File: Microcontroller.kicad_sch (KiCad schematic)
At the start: 33 parts, among them J501 USB4105-GF-A, J502 TC2030-CTX, SW501 PTS526SK15SMTR2 LFS, U501 USBLC6-2SC6, U502 STM32G441KBT6, Y501 ATS08A-E

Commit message: feat: checked REV A
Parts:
- removed J502: TC2030-CTX, Connector:Tag-Connect_TC2030-IDC-NL_2x03_P1.27mm_Vertical, symbol Connector:Conn_ARM_SWD_TagConnect_TC2030-NL
- added F501: MF-MSMF030-2, Resistor_SMD:R_1812_4532Metric, symbol Device:Polyfuse_Small
- added J501: Conn_ST_STDC14, Connector_PinHeader_1.27mm:PinHeader_2x07_P1.27mm_Vertical_SMD, symbol Connector:Conn_ST_STDC14
- FB501: value ?UNKWN? -> MH1608-601Y; footprint (none) -> Inductor_SMD:L_0603_1608Metric; Impedance (none) -> 600R @ 100MHz; MPN (none) -> MH1608-601Y; Manufacturer (none) -> Bourns Inc.; SPN (none) -> MH1608-601YCT-ND; Supplier (none) -> DigiKey
- renumbered C506 to C504, C504 to C505, C507 to C506, C508 to C507, C505 to C508, C515 to C510, C516 to C511, C510 to C512, J501 to J502, R510 to R503, R509 to R504, R507 to R505, R508 to R506, R503 to R507, R505 to R508, R504 to R509, R506 to R510, U502 to U501, U501 to U502
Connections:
- net +3V0: now also J501.3 (VCC)
- net GND: now also J501.5 (GND), J501.7 (GND)
- net VBUS: now also F501.2; no longer J502.A4 (VBUS), J502.A9 (VBUS), J502.B4 (VBUS), J502.B9 (VBUS)
- net at R504.1: now also J501.4 (JTMS/SWDIO)
- net at R505.1: now also J501.12 (~{RST})
- net at R503.1: now also J501.6 (JCLK/SWCLK)
- net at R506.1: now also J501.8 (JTDO/SWO)
- new net VBUS_RAW: F501.1, J502.A4 (VBUS), J502.A9 (VBUS), J502.B4 (VBUS), J502.B9 (VBUS)
- no-connect marks 12 -> 17
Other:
- note removed: "Unknown if there is an available part"
- moved on the sheet: C501, C502, C503, C504, C505, C506, C507, C508, C509, C510, C511, C512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

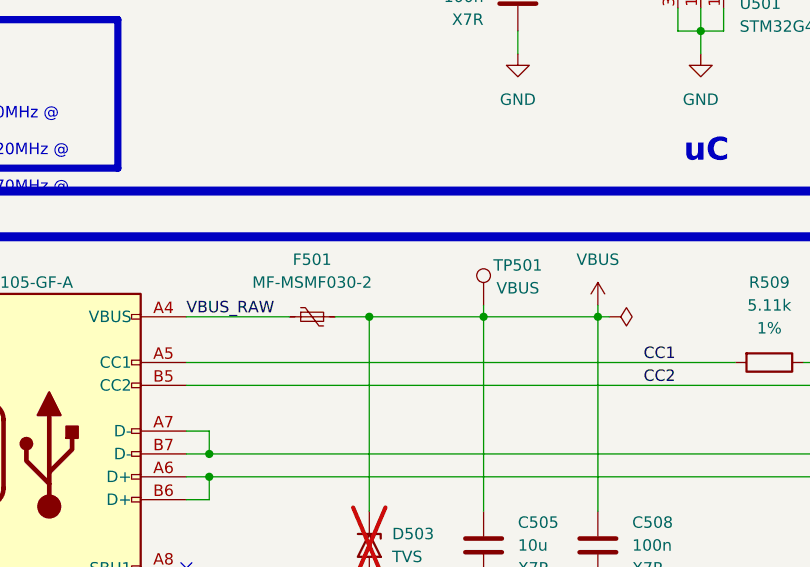
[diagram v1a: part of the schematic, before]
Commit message: fix: net naming, NC STM32 pins, silkscreen, pin 1 indicator
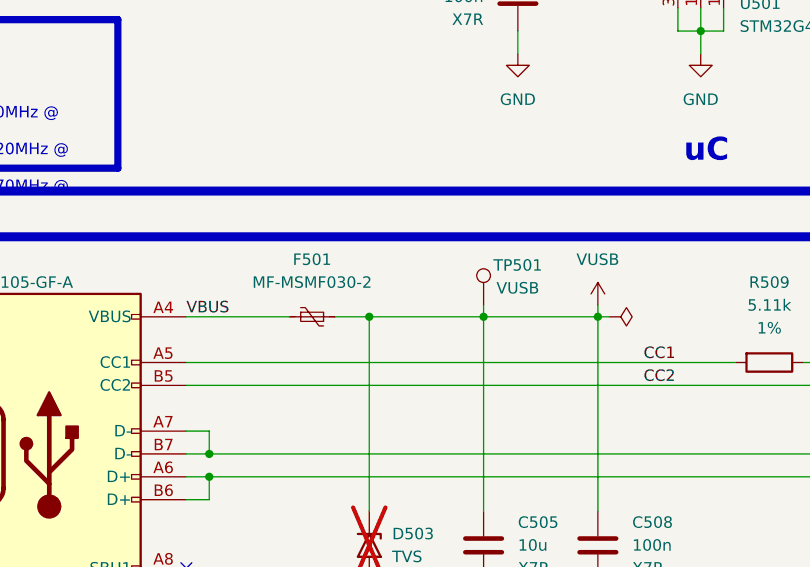
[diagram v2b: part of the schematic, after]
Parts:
- TP501: value VBUS -> VUSB
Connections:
- net VBUS_RAW is gone; now on net VBUS: F501.1, J502.A4 (VBUS), J502.A9 (VBUS), J502.B4 (VBUS), J502.B9 (VBUS)
- net VBUS: no longer C505.1, C508.1, D503.1 (A1), F501.2, TP501.1
- new net VUSB: C505.1, C508.1, D503.1 (A1), F501.2, TP501.1
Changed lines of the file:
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@@
 		)
 	)
-	(label "VBUS_RAW"
+	(label "VBUS"
 		(at 201.93 160.02 0)
 		(effects
@@
 			)
 		)
-		(property "Value" "VBUS"
+		(property "Value" "VUSB"
 			(at 238.76 156.845 0)
 			(effects
@@
 			)
 		)
-		(property "Value" "VBUS"
+		(property "Value" "VUSB"
 			(at 247.65 153.67 0)
 			(effects
@@
 			)
 		)
-		(property "Description" "Power symbol creates a global label with name \"VBUS\""
+		(property "Description" "Power symbol creates a global label with name \"VUSB\""
 			(at 247.65 158.75 0)
 			(effects
